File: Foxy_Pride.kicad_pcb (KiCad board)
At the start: 2 copper layers, 89.3 x 67.9 mm, 34 parts, among them U1 TLC555CDR, U2 74HC4017D

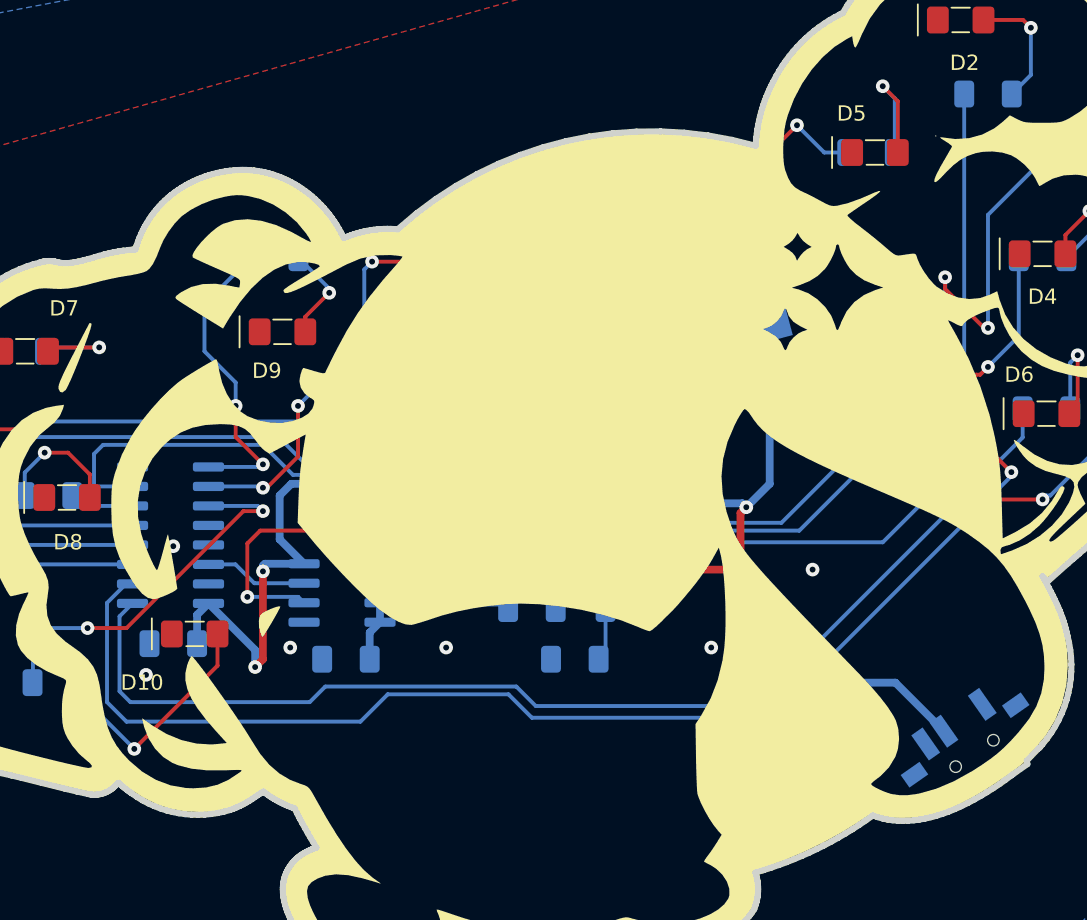
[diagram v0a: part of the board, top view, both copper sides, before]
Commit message: changes to make some routing shorter, fixed switch and power, added eyes in copper
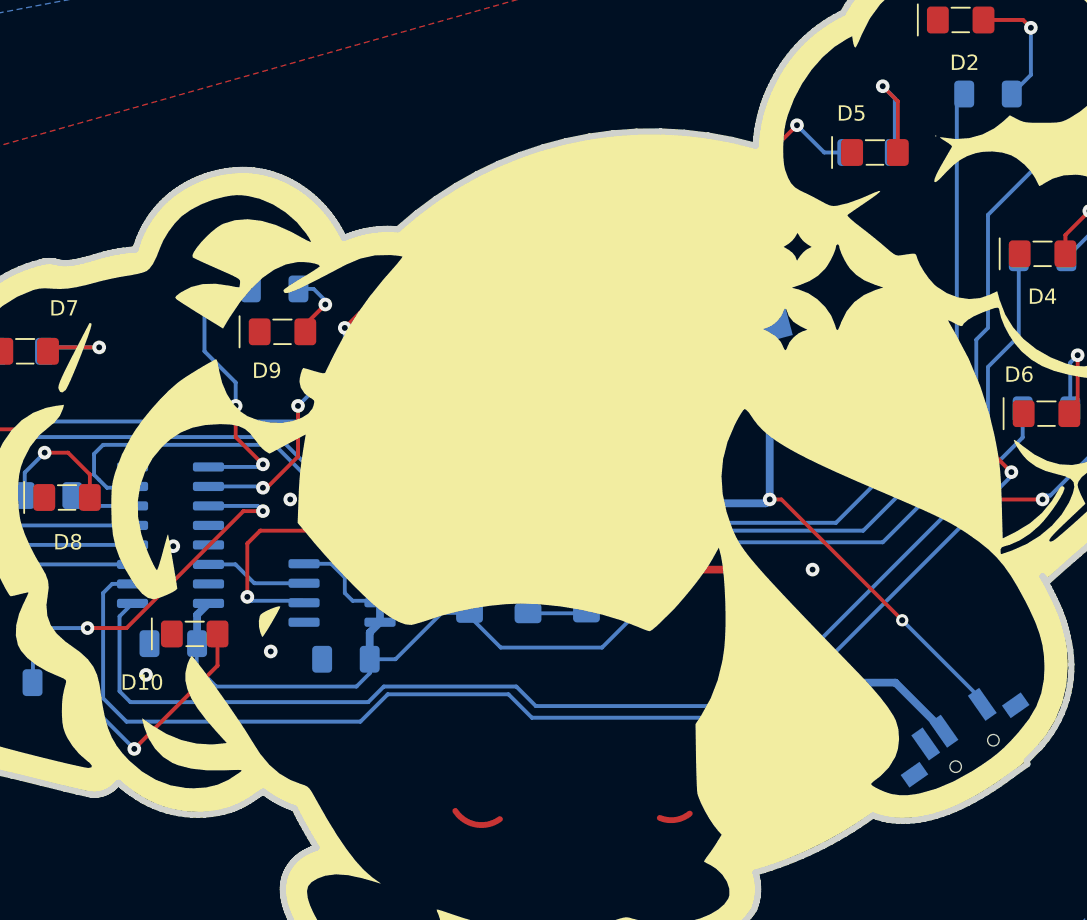
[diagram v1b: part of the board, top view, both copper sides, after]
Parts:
- moved R2 6.72 mm to (65.5, 76.7), turned to -90 degrees
- moved C1 4.66 mm to (69.3, 76.7), turned to 90 degrees
- moved R1 4.26 mm to (61.7, 76.7), turned to 90 degrees
- moved R11 2.03 mm to (49.0, 57.1)
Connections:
- BT1 pad 1: +3V -> +Vbatt
- S1 pad 1: GND -> +Vbatt
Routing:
- net +3V: track 147.2 -> 74.2 mm, vias 5 -> 2
- net +Vbatt: track 0.00 -> 62.6 mm, vias 0 -> 2
- net Net-(R1-Pad2): track 46.7 -> 30.2 mm, vias 4 -> 2
- net Net-(R3-Pad2): track 121.3 -> 118.2 mm, vias 4 -> 2
- net Net-(R6-Pad2): track 82.7 -> 81.0 mm, vias 2 -> 0
- net Net-(D9-Pad2): track 6.30 -> 4.64 mm
- net Net-(R7-Pad2): track 56.8 -> 55.3 mm
- net Net-(R11-Pad2): track 19.9 -> 19.1 mm
- net Net-(R4-Pad2): track 102.6 -> 103.3 mm
- net GND: vias 6 -> 11

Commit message: Finalized design and layout on Foxy Pride PCB
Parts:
- added G***: LOGO, FoxyPride:Robyn Edit tip of tail 0.73x0.72, F.Cu at (87.4, 74.0)
- added G***: LOGO, FoxyPride:Robyn Edit Ears 1.09x.36, F.Cu at (64.1, 80.1)
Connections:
- S1 pad : (no net) -> GND
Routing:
- net +Vbatt: track 62.6 -> 72.5 mm
- net +3V: track 74.2 -> 77.0 mm
- net GND: vias 11 -> 10
